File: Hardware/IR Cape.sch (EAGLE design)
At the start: 32 parts, among them T3 MPSA13RLRAG, T4 MPSA13RLRAG, T5 MPSA13RLRAG, X1 KLBR2, X2 KLBR2, X3 KLBR2

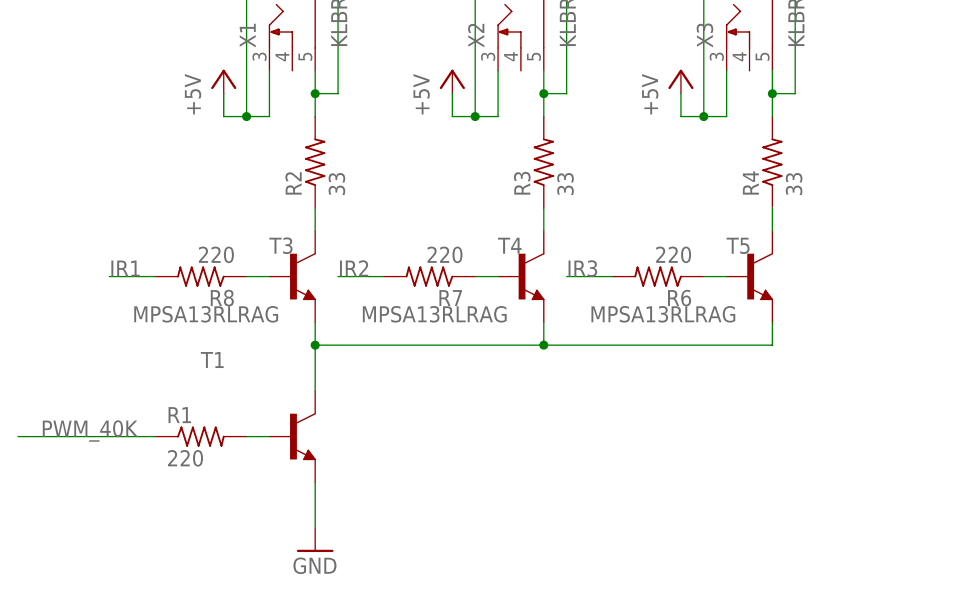
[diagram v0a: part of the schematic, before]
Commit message: Fixed resistor values in schematic
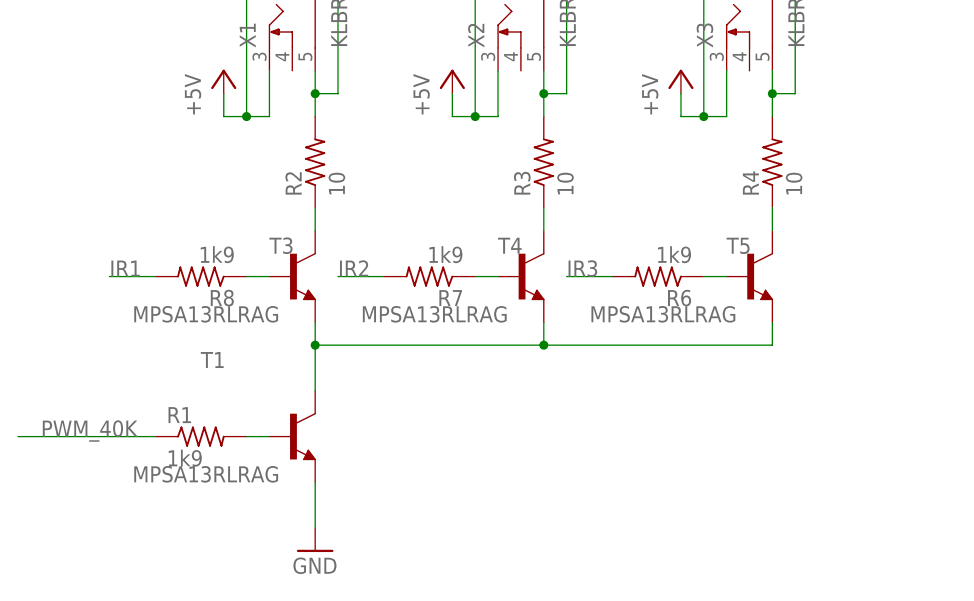
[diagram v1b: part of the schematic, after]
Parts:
- R1, R6, R7, R8: value 220 -> 1k9
- R2, R3, R4: value 33 -> 10
- T1: value (none) -> MPSA13RLRAG
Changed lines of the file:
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@@
 <grid distance="0.1" unitdist="inch" unit="inch" style="lines" multiple="1" display="no" altdistance="0.01" altunitdist="inch" altunit="inch"/>
 <layers>
-<layer number="1" name="Top" color="4" fill="1" visible="yes" active="no"/>
-<layer number="16" name="Bottom" color="1" fill="1" visible="yes" active="no"/>
-<layer number="17" name="Pads" color="2" fill="1" visible="yes" active="no"/>
-<layer number="18" name="Vias" color="14" fill="1" visible="yes" active="no"/>
-<layer number="19" name="Unrouted" color="6" fill="1" visible="yes" active="no"/>
-<layer number="20" name="Dimension" color="15" fill="1" visible="yes" active="no"/>
-<layer number="21" name="tPlace" color="7" fill="1" visible="yes" active="no"/>
-<layer number="22" name="bPlace" color="7" fill="1" visible="yes" active="no"/>
-<layer number="23" name="tOrigins" color="15" fill="1" visible="yes" active="no"/>
-<layer number="24" name="bOrigins" color="15" fill="1" visible="yes" active="no"/>
-<layer number="25" name="tNames" color="7" fill="1" visible="yes" active="no"/>
-<layer number="26" name="bNames" color="7" fill="1" visible="yes" active="no"/>
-<layer number="27" name="tValues" color="7" fill="1" visible="yes" active="no"/>
-<layer number="28" name="bValues" color="7" fill="1" visible="yes" active="no"/>
+<layer number="1" name="Top" color="4" fill="1" visible="no" active="no"/>
+<layer number="16" name="Bottom" color="1" fill="1" visible="no" active="no"/>
+<layer number="17" name="Pads" color="2" fill="1" visible="no" active="no"/>
+<layer number="18" name="Vias" color="14" fill="1" visible="no" active="no"/>
+<layer number="19" name="Unrouted" color="6" fill="1" visible="no" active="no"/>
+<layer number="20" name="Dimension" color="15" fill="1" visible="no" active="no"/>
+<layer number="21" name="tPlace" color="7" fill="1" visible="no" active="no"/>
+<layer number="22" name="bPlace" color="7" fill="1" visible="no" active="no"/>
+<layer number="23" name="tOrigins" color="15" fill="1" visible="no" active="no"/>
+<layer number="24" name="bOrigins" color="15" fill="1" visible="no" active="no"/>
+<layer number="25" name="tNames" color="7" fill="1" visible="no" active="no"/>
+<layer number="26" name="bNames" color="7" fill="1" visible="no" active="no"/>
+<layer number="27" name="tValues" color="7" fill="1" visible="no" active="no"/>
+<layer number="28" name="bValues" color="7" fill="1" visible="no" active="no"/>
 <layer number="29" name="tStop" color="7" fill="3" visible="no" active="no"/>
 <layer number="30" name="bStop" color="7" fill="6" visible="no" active="no"/>
@@
 <layer number="35" name="tGlue" color="7" fill="4" visible="no" active="no"/>
 <layer number="36" name="bGlue" color="7" fill="5" visible="no" active="no"/>
-<layer number="37" name="tTest" color="7" fill="1" visible="yes" active="no"/>
-<layer number="38" name="bTest" color="7" fill="1" visible="yes" active="no"/>
+<layer number="37" name="tTest" color="7" fill="1" visible="no" active="no"/>
+<layer number="38" name="bTest" color="7" fill="1" visible="no" active="no"/>
 <layer number="39" name="tKeepout" color="4" fill="11" visible="no" active="no"/>
 <layer number="40" name="bKeepout" color="1" fill="11" visible="no" active="no"/>
@@
 <layer number="44" name="Drills" color="7" fill="1" visible="no" active="no"/>
 <layer number="45" name="Holes" color="7" fill="1" visible="no" active="no"/>
-<layer number="46" name="Milling" color="3" fill="1" visible="yes" active="no"/>
-<layer number="47" name="Measures" color="7" fill="1" visible="yes" active="no"/>
-<layer number="48" name="Document" color="7" fill="1" visible="yes" active="no"/>
-<layer number="49" name="Reference" color="7" fill="1" visible="yes" active="no"/>
-<layer number="50" name="dxf" color="7" fill="1" visible="yes" active="no"/>
-<layer number="51" name="tDocu" color="7" fill="1" visible="yes" active="no"/>
-<layer number="52" name="bDocu" color="7" fill="1" visible="yes" active="no"/>
-<layer number="53" name="tGND_GNDA" color="7" fill="9" visible="yes" active="no"/>
-<layer number="54" name="bGND_GNDA" color="1" fill="9" visible="yes" active="no"/>
-<layer number="56" name="wert" color="7" fill="1" visible="yes" active="no"/>
-<layer number="57" name="tCAD" color="7" fill="1" visible="yes" active="no"/>
+<layer number="46" name="Milling" color="3" fill="1" visible="no" active="no"/>
+<layer number="47" name="Measures" color="7" fill="1" visible="no" active="no"/>
+<layer number="48" name="Document" color="7" fill="1" visible="no" active="no"/>
+<layer number="49" name="Reference" color="7" fill="1" visible="no" active="no"/>
+<layer number="50" name="dxf" color="7" fill="1" visible="no" active="no"/>
+<layer number="51" name="tDocu" color="7" fill="1" visible="no" active="no"/>
+<layer number="52" name="bDocu" color="7" fill="1" visible="no" active="no"/>
+<layer number="53" name="tGND_GNDA" color="7" fill="9" visible="no" active="no"/>
+<layer number="54" name="bGND_GNDA" color="1" fill="9" visible="no" active="no"/>
+<layer number="56" name="wert" color="7" fill="1" visible="no" active="no"/>
+<layer number="57" name="tCAD" color="7" fill="1" visible="no" active="no"/>
 <layer number="91" name="Nets" color="2" fill="1" visible="yes" active="yes"/>
 <layer number="92" name="Busses" color="1" fill="1" visible="yes" active="yes"/>
@@
 </classes>
 <parts>
-<part name="T1" library="transistor-neu-to92" deviceset="*-NPN-" device="TO92-EBC" technology="2N2222"/>
-<part name="R1" library="resistor" deviceset="R-US_" device="0207/10" value="220"/>
+<part name="T1" library="transistor-neu-to92" deviceset="*-NPN-" device="TO92-EBC" technology="2N2222" value="MPSA13RLRAG"/>
+<part name="R1" library="resistor" deviceset="R-US_" device="0207/10" value="1k9"/>
 <part name="GND1" library="supply1" deviceset="GND" device=""/>
 <part name="U$1" library="adafruit" deviceset="BEAGLEBONE_OUTLINE" device="" value=""/>
-<part name="R2" library="resistor" deviceset="R-US_" device="0207/10" value="33"/>
-<part name="R3" library="resistor" deviceset="R-US_" device="0207/10" value="33"/>
-<part name="R4" library="resistor" deviceset="R-US_" device="0207/10" value="33"/>
+<part name="R2" library="resistor" deviceset="R-US_" device="0207/10" value="10"/>
+<part name="R3" library="resistor" deviceset="R-US_" device="0207/10" value="10"/>
+<part name="R4" library="resistor" deviceset="R-US_" device="0207/10" value="10"/>
 <part name="GND2" library="supply1" deviceset="GND" device=""/>
 <part name="T3" library="transistor-neu-to92" deviceset="*-NPN-" device="TO92-EBC" technology="2N2222" value="MPSA13RLRAG"/>
@@
 <part name="P+5" library="supply1" deviceset="+5V" device=""/>
 <part name="+3V3" library="supply1" deviceset="+3V3" device=""/>
-<part name="R6" library="resistor" deviceset="R-US_" device="0207/10" value="220"/>
-<part name="R7" library="resistor" deviceset="R-US_" device="0207/10" value="220"/>
-<part name="R8" library="resistor" deviceset="R-US_" device="0207/10" value="220"/>
+<part name="R6" library="resistor" deviceset="R-US_" device="0207/10" value="1k9"/>
+<part name="R7" library="resistor" deviceset="R-US_" device="0207/10" value="1k9"/>
+<part name="R8" library="resistor" deviceset="R-US_" device="0207/10" value="1k9"/>
 <part name="C2" library="adafruit" deviceset="CPOL-US" device="E2-5" value="10uF"/>
 <part name="P+6" library="supply1" deviceset="+5V" device=""/>
@@
 </plain>
 <instances>
-<instance part="T1" gate="G$1" x="35.56" y="22.86"/>
+<instance part="T1" gate="G$1" x="35.56" y="22.86" smashed="yes">
+<attribute name="NAME" x="25.4" y="30.48" size="1.778" layer="95"/>
+<attribute name="VALUE" x="17.78" y="17.78" size="1.778" layer="96"/>
+</instance>
 <instance part="R1" gate="G$1" x="25.4" y="22.86"/>
 <instance part="GND1" gate="1" x="139.7" y="63.5"/>
